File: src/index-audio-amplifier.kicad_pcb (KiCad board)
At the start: 2 copper layers, 23.5 x 23.5 mm, 59 parts, among them J1 CU3616SASCLA004-LF, J2 SWD_PicoprobeCandybar, J3 Conn_01x02, J4 Conn_01x02, U1 RP2040, U2 NCP167, U3 W25Q16JVUXIQ, U4 MAX98360CENL, U5 NCP167, U6 MAX98360CENL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

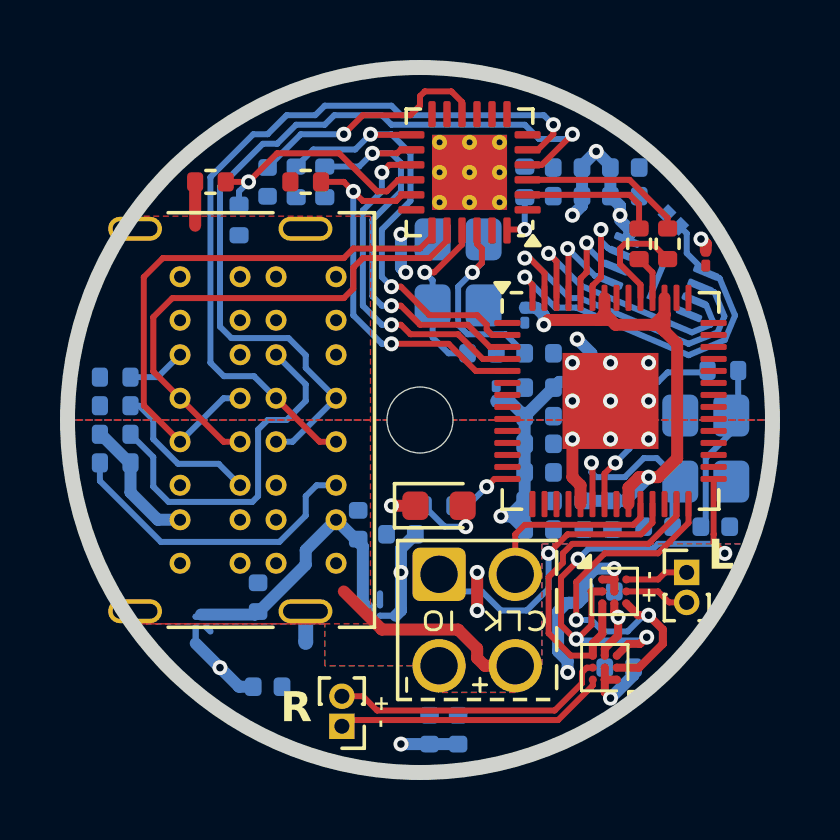
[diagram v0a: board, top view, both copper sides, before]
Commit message: Give capacitors a tad more space under USB port
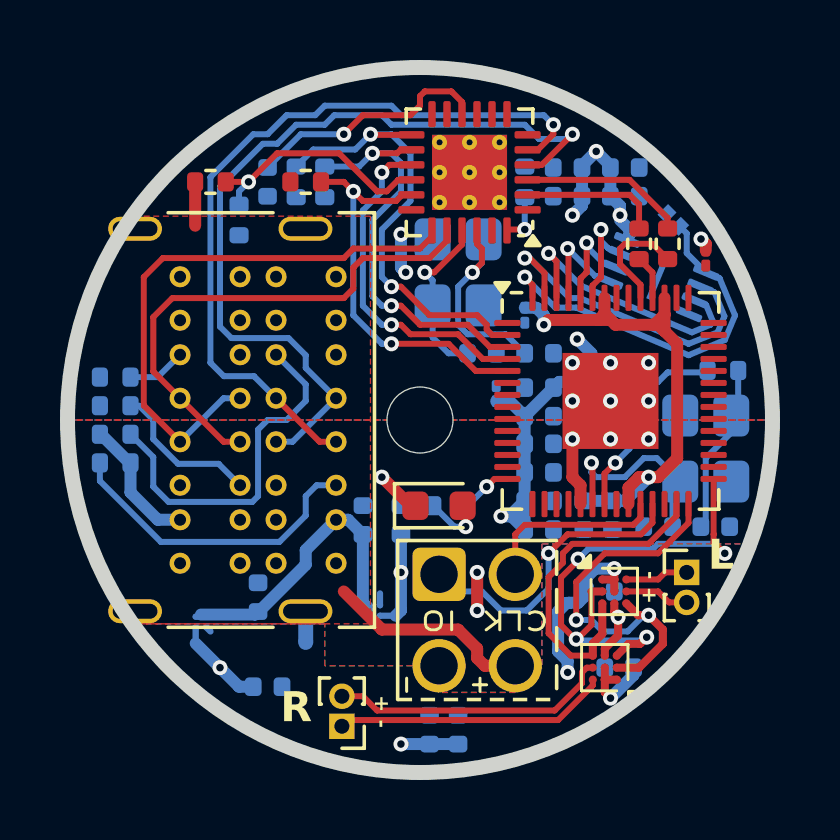
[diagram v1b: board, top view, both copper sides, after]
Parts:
- moved C2 0.48 mm to (147.9, 73.3), turned to 90 degrees
- moved R3 0.32 mm to (149.5, 72.9)
- moved C1 0.22 mm to (146.6, 73.3)
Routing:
- net GND: track 8.90 -> 9.61 mm
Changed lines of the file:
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@@
 	(footprint "Resistor_SMD:R_0402_1005Metric"
 		(layer "B.Cu")
-		(at 149.135 72.8575 180)
+		(at 149.4525 72.8575 180)
 		(descr "Resistor SMD 0402 (1005 Metric), square (rectangular) end terminal, IPC-7351 nominal, (Body size source: IPC-SM-782 page 72, https://www.pcb-3d.com/wordpress/wp-content/uploads/ipc-sm-782a_amendment_1_and_2.pdf), generated with kicad-footprint-generator")
 		(tags "resistor")
@@
 	(footprint "Capacitor_SMD:C_0402_1005Metric"
 		(layer "B.Cu")
-		(at 147.865 73.81 180)
+		(at 147.865 73.33375 90)
 		(descr "Capacitor SMD 0402 (1005 Metric), square (rectangular) end terminal, IPC-7351 nominal, (Body size source: IPC-SM-782 page 76, https://www.pcb-3d.com/wordpress/wp-content/uploads/ipc-sm-782a_amendment_1_and_2.pdf), generated with kicad-footprint-generator")
 		(tags "capacitor")
 		(property "Reference" "C2"
-			(at 0 1.16 0)
+			(at 0 1.16 90)
 			(layer "B.SilkS")
 			(hide yes)
@@
 		)
 		(property "Value" "1u"
-			(at 0 -1.16 0)
+			(at 0 -1.16 90)
 			(layer "B.Fab")
 			(effects
@@
 		)
 		(property "Datasheet" "~"
-			(at 0 0 0)
+			(at 0 0 90)
 			(layer "B.Fab")
 			(hide yes)
@@
 		)
 		(property "Description" "Unpolarized capacitor"
-			(at 0 0 0)
+			(at 0 0 90)
 			(layer "B.Fab")
 			(hide yes)
@@
 		(attr smd)
 		(fp_line
-			(start -0.107836 0.36)
-			(end 0.107836 0.36)
+			(start -0.107836 -0.36)
+			(end 0.107836 -0.36)
 			(stroke
 				(width 0.12)
@@
 		)
 		(fp_line
-			(start -0.107836 -0.36)
-			(end 0.107836 -0.36)
+			(start -0.107836 0.36)
+			(end 0.107836 0.36)
 			(stroke
 				(width 0.12)
@@
 		)
 		(fp_line
-			(start 0.91 0.46)
-			(end 0.91 -0.46)
+			(start 0.91 -0.46)
+			(end -0.91 -0.46)
 			(stroke
 				(width 0.05)
@@
 		)
 		(fp_line
-			(start 0.91 -0.46)
-			(end -0.91 -0.46)
+			(start -0.91 -0.46)
+			(end -0.91 0.46)
 			(stroke
 				(width 0.05)
@@
 		)
 		(fp_line
-			(start -0.91 0.46)
-			(end 0.91 0.46)
+			(start 0.91 0.46)
+			(end 0.91 -0.46)
 			(stroke
 				(width 0.05)
@@
 		)
 		(fp_line
-			(start -0.91 -0.46)
-			(end -0.91 0.46)
+			(start -0.91 0.46)
+			(end 0.91 0.46)
 			(stroke
 				(width 0.05)
@@
 		)
 		(fp_line
-			(start 0.5 0.25)
-			(end 0.5 -0.25)
+			(start 0.5 -0.25)
+			(end -0.5 -0.25)
 			(stroke
 				(width 0.1)
@@
 		)
 		(fp_line
-			(start 0.5 -0.25)
-			(end -0.5 -0.25)
+			(start -0.5 -0.25)
+			(end -0.5 0.25)
 			(stroke
 				(width 0.1)
@@
 		)
 		(fp_line
-			(start -0.5 0.25)
-			(end 0.5 0.25)
+			(start 0.5 0.25)
+			(end 0.5 -0.25)
 			(stroke
 				(width 0.1)
@@
 		)
 		(fp_line
-			(start -0.5 -0.25)
-			(end -0.5 0.25)
+			(start -0.5 0.25)
+			(end 0.5 0.25)
 			(stroke
 				(width 0.1)
@@
 		)
 		(fp_text user "${REFERENCE}"
-			(at 0 0 0)
+			(at 0 0 90)
 			(layer "B.Fab")
 			(effects
@@
 		)
 		(pad "1" smd roundrect
-			(at -0.48 0 180)
+			(at -0.48 0 90)
 			(size 0.56 0.62)
 			(layers "B.Cu" "B.Mask" "B.Paste")
@@
 		)
 		(pad "2" smd roundrect
-			(at 0.48 0 180)
+			(at 0.48 0 90)
 			(size 0.56 0.62)
 			(layers "B.Cu" "B.Mask" "B.Paste")
@@
 	(footprint "Capacitor_SMD:C_0402_1005Metric"
 		(layer "B.Cu")
-		(at 146.44 73.4925 90)
+		(at 146.595 73.33375 90)
 		(descr "Capacitor SMD 0402 (1005 Metric), square (rectangular) end terminal, IPC-7351 nominal, (Body size source: IPC-SM-782 page 76, https://www.pcb-3d.com/wordpress/wp-content/uploads/ipc-sm-782a_amendment_1_and_2.pdf), generated with kicad-footprint-generator")
 		(tags "capacitor")
@@
 	)
 	(segment
-		(start 150.405 76.35)
-		(end 150.405 75.08)
+		(start 147.23 71.905)
+		(end 148.1825 72.8575)
 		(width 0.4)
 		(layer "F.Cu")
@@
 	)
 	(segment
-		(start 148.3475 72.8575)
-		(end 147.5475 72.8575)
+		(start 150.405 76.35)
+		(end 150.405 75.08)
 		(width 0.4)
 		(layer "F.Cu")
@@
 		(net 1)
 	)
+	(segment
+		(start 148.1825 72.8575)
+		(end 148.3475 72.8575)
+		(width 0.4)
+		(layer "F.Cu")
+		(net 1)
+	)
 	(via
 		(at 153.58 68.095)
@@
 	)
 	(via
-		(at 147.5475 72.8575)
+		(at 147.23 71.905)
 		(size 0.5)
 		(drill 0.25)
@@
 	)
 	(segment
-		(start 147.865 74.29)
-		(end 147.865 75.08)
-		(width 0.4)
-		(layer "B.Cu")
-		(net 2)
-	)
-	(segment
 		(start 147.865 76.35)
 		(end 147.69 76.525)
@@
 	)
 	(segment
-		(start 148.345 73.81)
-		(end 147.865 74.29)
-		(width 0.4)
-		(layer "B.Cu")
-		(net 2)
-	)
-	(segment
 		(start 154.215 68.4125)
 		(end 153.8975 68.73)
@@
 	)
 	(segment
+		(start 147.865 73.81375)
+		(end 147.865 75.08)
+		(width 0.4)
+		(layer "B.Cu")
+		(net 2)
+	)
+	(segment
 		(start 153.8975 68.73)
 		(end 153.13925 68.73)
@@
 	)
 	(segment
-		(start 150.024 73.556)
-		(end 149.3235 73.556)
+		(start 148.9445 72.8575)
+		(end 148.9425 72.8575)
 		(width 0.2)
 		(layer "B.Cu")
@@
 	)
 	(segment
-		(start 149.3235 73.556)
-		(end 148.625 72.8575)
+		(start 149.643 73.556)
+		(end 148.9445 72.8575)
+		(width 0.2)
+		(layer "B.Cu")
+		(net 7)
+	)
+	(segment
+		(start 150.024 73.556)
+		(end 149.643 73.556)
 		(width 0.2)
 		(layer "B.Cu")
@@
 	)
 	(segment
+		(start 145.7025 73.325)
+		(end 146.10625 73.325)
+		(width 0.4)
+		(layer "B.Cu")
+		(net 17)
+	)
+	(segment
 		(start 138.81625 71.42875)
 		(end 138.85 71.42875)
@@
 	)
 	(segment
-		(start 146.44 73.9725)
-		(end 146.44 74.0625)
-		(width 0.4)
-		(layer "B.Cu")
-		(net 17)
-	)
-	(segment
 		(start 144.69 74.3375)
 		(end 145.7025 73.325)
@@
 	)
 	(segment
+		(start 146.10625 73.325)
+		(end 146.595 73.81375)
+		(width 0.4)
+		(layer "B.Cu")
+		(net 17)
+	)
+	(segment
 		(start 137.86375 70.47625)
 		(end 138.81625 71.42875)
@@
 	)
 	(segment
-		(start 145.7025 73.325)
-		(end 146.35 73.9725)
+		(start 146.595 73.81375)
+		(end 146.595 76.096)
 		(width 0.4)
 		(layer "B.Cu")
@@
 	)
 	(segment
-		(start 146.35 73.9725)
-		(end 146.44 73.9725)
-		(width 0.4)
-		(layer "B.Cu")
-		(net 17)
-	)
-	(segment
-		(start 146.44 74.0625)
-		(end 146.595 74.2175)
-		(width 0.4)
-		(layer "B.Cu")
-		(net 17)
-	)
-	(segment
 		(start 146.8165 76.525)
 		(end 146.8165 76.175)
@@
 	)
 	(segment
-		(start 146.595 74.2175)
-		(end 146.595 76.096)
-		(width 0.4)
-		(layer "B.Cu")
-		(net 17)
-	)
-	(segment
 		(start 153.58 60.475)
 		(end 152.56 61.495)
@@
 	)
 	(segment
-		(start 149.645 72.8575)
+		(start 149.9625 72.8575)
 		(end 150.0875 72.8575)
 		(width 0.2)

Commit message: Mildly improve Fab layer text readability
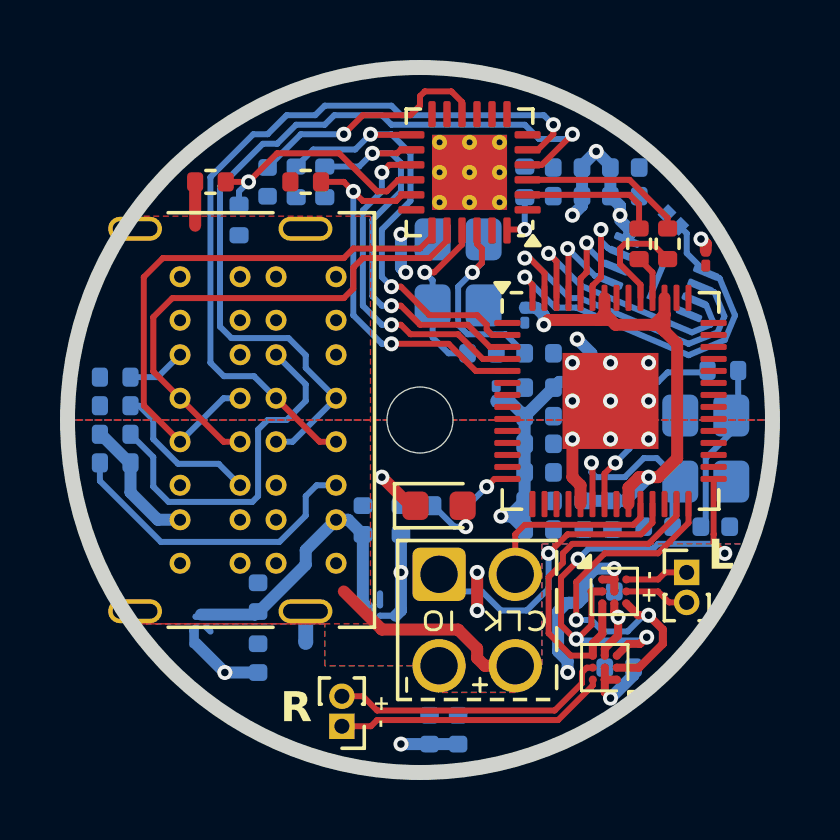
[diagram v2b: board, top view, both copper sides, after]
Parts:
- moved C102 1.00 mm to (143.1, 77.9), turned to 90 degrees
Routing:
- net +3V3A: track 13.9 -> 14.5 mm

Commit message: Add silkscreen text and USB Hub bypass test points
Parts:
- added TP1: TestPoint_Small, ProjectFootprints_IndexAudioAmplifier:TestPoint_Pad_D0.5mm, F.Cu at (154.5, 62.5)
- added TP2: TestPoint_Small, ProjectFootprints_IndexAudioAmplifier:TestPoint_Pad_D0.5mm, F.Cu at (153.3, 62.0)
- added TP3: TestPoint_Small, ProjectFootprints_IndexAudioAmplifier:TestPoint_Pad_D0.5mm, F.Cu at (148.8, 64.8)
- added TP4: TestPoint_Small, ProjectFootprints_IndexAudioAmplifier:TestPoint_Pad_D0.5mm, F.Cu at (149.3, 65.6)
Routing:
- net /DP_IN: track 17.3 -> 19.2 mm
- net /DM_IN: track 19.0 -> 20.1 mm
- net Net-(U7-XTALIN): track 7.41 -> 8.52 mm
- net /HUB_SMCK: track 14.2 -> 13.6 mm
- net /HUB_SUSP: track 13.4 -> 14.0 mm
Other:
- board text added: "BOOTSEL"
- board text added: "Lower: →Audio in"
- board text added: "Peter S. Hollander, 2025"
- board text added: "Upper: ←Aux. device"
- board text added: "XX/XX/XX Rev 0"
- board text added: "gitlab.com/recursivenomad/"
- board text added: "index-audio-amplifier"
